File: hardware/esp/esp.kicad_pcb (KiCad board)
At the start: 2 copper layers, 100 x 80 mm, 88 parts, among them J1 Conn_01x02, J2 USB_C_Receptacle_USB2.0_16P, J3 USB_C_Receptacle_USB2.0_16P, J4 Conn_01x02, J5 Conn_Coaxial, J6 Conn_01x09_Pin, J7 Conn_01x06_Pin, J8 Conn_01x09_Pin, SW1 RESET, SW2 BOOT, U1 AMS1117-3.3, U2 CP2102N-Axx-xQFN20, U3 ESP32-S3-WROOM-1, U4 VL53L0X, U5 NRF24L01, U6 BME280, Y1 16MHz

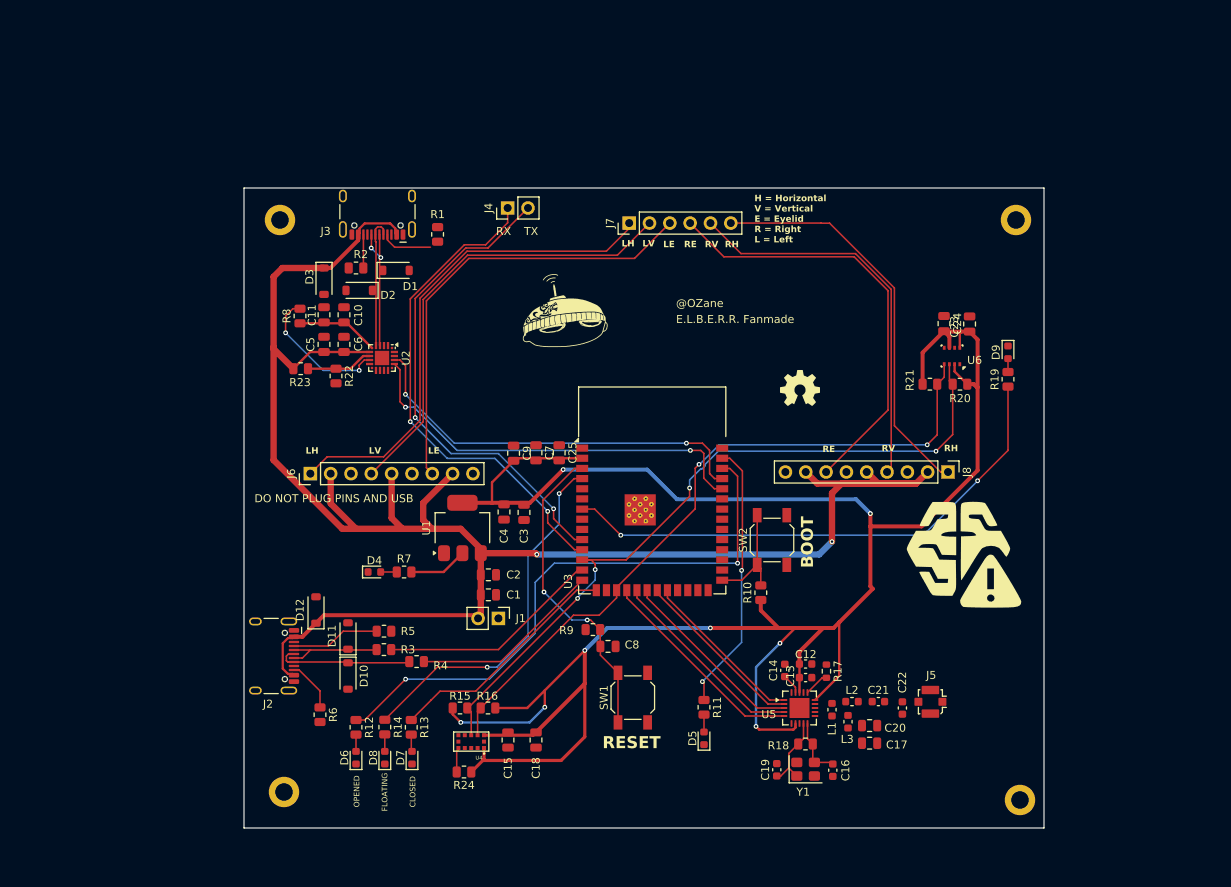
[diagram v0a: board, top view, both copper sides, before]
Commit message: Placing mounting holes, routing impedance matching drace
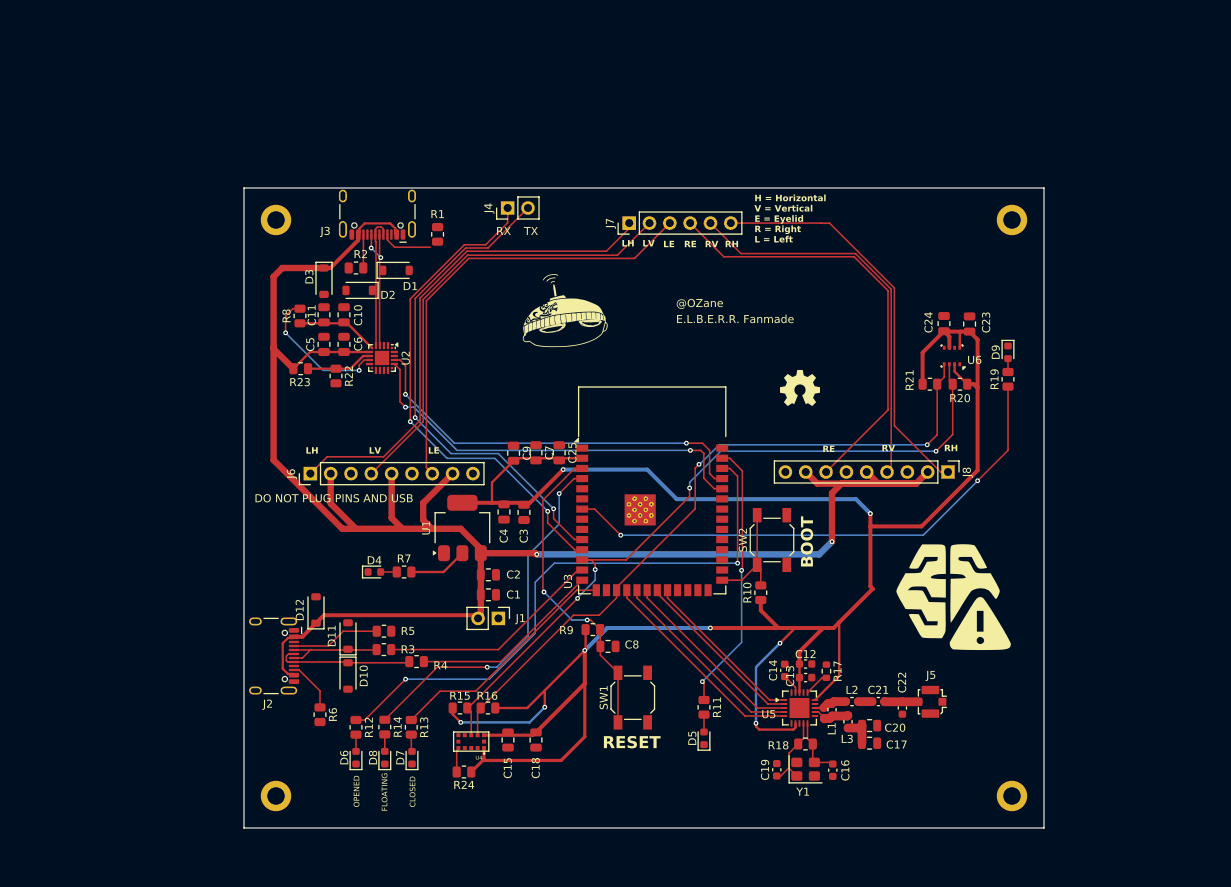
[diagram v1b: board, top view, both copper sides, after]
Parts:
- moved G*** 5.46 mm to (173.7, 121.3)
- moved REF** 1.12 mm to (89.0, 146.0)
- moved REF** 1.12 mm to (181.0, 146.0)
- moved REF** 0.50 mm to (89.0, 74.0)
- moved REF** 0.50 mm to (181.0, 74.0)
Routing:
- net Net-(U5-ANT1): track 0.00 -> 4.74 mm
- net Net-(J5-In): track 0.00 -> 4.24 mm
- net Net-(U5-ANT2): track 0.00 -> 4.12 mm
- net Net-(U5-VDD_PA): track 0.00 -> 4.07 mm
- net +3V3: track 298.5 -> 301.1 mm
- net Net-(C21-Pad1): track 0.00 -> 1.74 mm

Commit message: Updating BOM, adding fixes to the PCB and silkscreen finishes
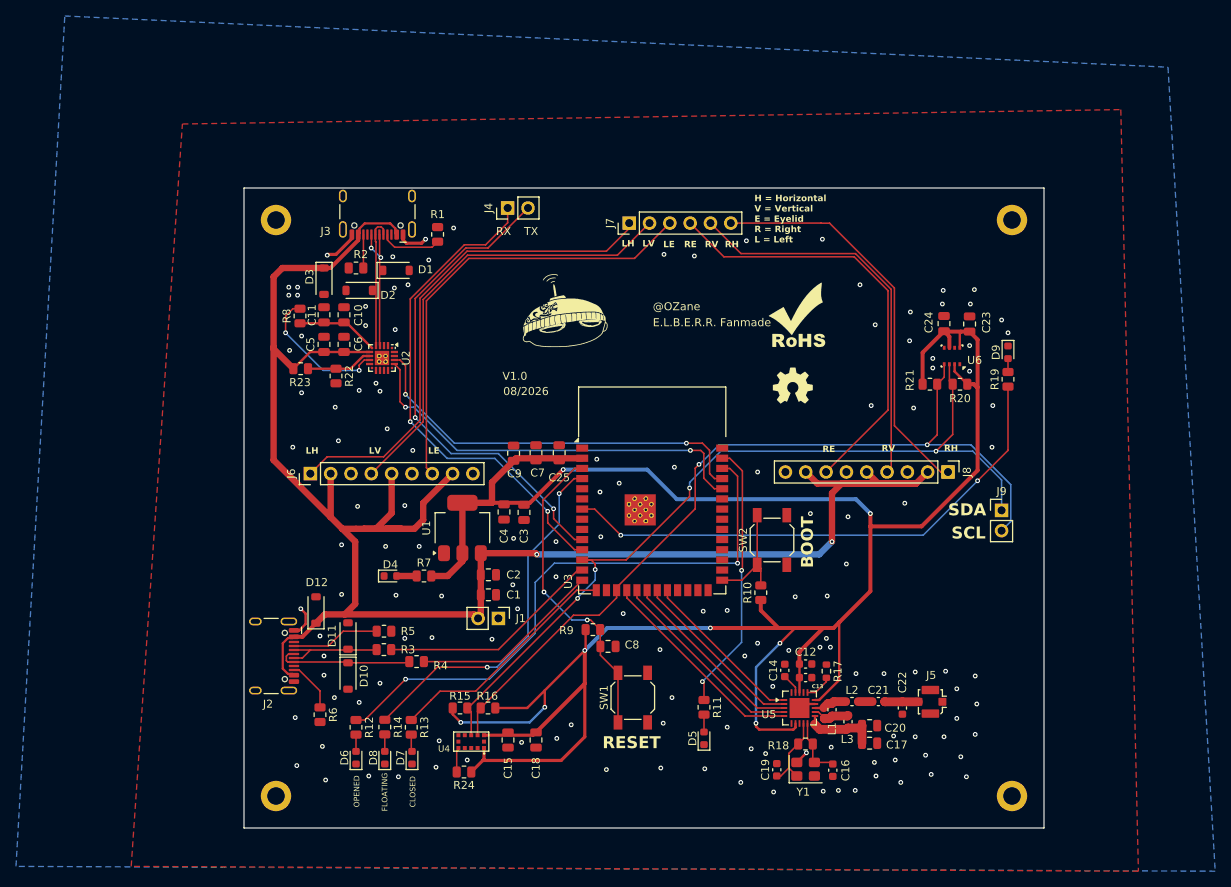
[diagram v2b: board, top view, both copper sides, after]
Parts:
- added ?: , , F.Cu at (102.7, 91.0)
- added ?: , , F.Cu at (102.7, 91.7)
- added ?: , , F.Cu at (101.9, 91.7)
- added ?: , , F.Cu at (101.9, 91.0)
- added G***: LOGO, LOGO, F.Cu at (154.3, 86.1)
- added J9: Conn_01x02, Connector_PinHeader_2.54mm:PinHeader_1x02_P2.54mm_Vertical, F.Cu at (179.7, 110.3)
- R11, R12, R13, R14, R19, R7: value R -> 1k
- moved R7 2.54 mm to (107.5, 118.5)
- moved D4 2.06 mm to (103.3, 118.5)
- moved G*** 1.64 mm to (172.3, 122.2)
- moved G*** 0.95 mm to (153.6, 94.7)
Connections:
- U3 pad 18: unconnected-(U3-IO10-Pad18) -> MISO
- U3 pad 21: MISO -> NRF_CSN
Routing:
- net SCL: track 87.7 -> 106.4 mm
- net GND: track 0.00 -> 16.1 mm, vias 0 -> 140
- net SDA: track 92.9 -> 106.4 mm
- net Net-(U5-VDD_PA): track 4.07 -> 9.64 mm
- net +5V: track 231.8 -> 236.9 mm
- net +3V3: track 301.1 -> 305.7 mm
- net Net-(J3-CC1): track 6.42 -> 7.61 mm
- added copper zone on B.Cu, net GND
- added copper zone on F.Cu, net GND
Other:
- board text added: "08/2026"
- board text added: "PAD RELIE AU PAD CENTRAL CAR SINON PAS D'ACCES AU GND"
- board text added: "SCL"
- board text added: "SDA"
- board text added: "V1.0"
- board text removed: "DO NOT PLUG PINS AND USB"
